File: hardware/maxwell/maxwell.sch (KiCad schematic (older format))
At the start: 29 parts

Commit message: Adding finalized PCB layout.
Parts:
- removed J?: Charger Output, symbol USB_A
- removed U?: MCP2515-I/ST, Housings_SSOP:TSSOP-20_4.4x6.5mm_Pitch0.65mm, symbol MCP2515-I/ST
- added J5: Charger Output, pbrook/Parts.pretty:JST-XH-4, symbol Conn_01x04
- added U1: MCP2515-E/ST-SOIC, Tinkerforge/kicad-libraries:SOIC-18, symbol MCP2515-E/ST-SOIC
- BZ1: renamed from BZ?; footprint (none) -> coddingtonbear/coddingtonbear.pretty:12mm_buzzer
- C1, C2, C3, C4, C5: renamed from C?; footprint (none) -> coddingtonbear/coddingtonbear.pretty:0805_Milling
- J1, J2: renamed from J?; footprint (none) -> pbrook/Parts.pretty:JST-XH-4
- J3: renamed from J?; footprint (none) -> pbrook/Parts.pretty:JST-XH-3
- J4: renamed from J?; footprint (none) -> KiCad/Pin_Headers.pretty:Pin_Header_Straight_2x03_Pitch2.54mm
- J6: renamed from J?; footprint (none) -> KiCad/Pin_Headers.pretty:Pin_Header_Straight_1x04_Pitch2.54mm
- Q1: renamed from Q?; footprint TO_SOT_Packages_SMD:SOT-23 -> adamgreig/agg-kicad/agg.pretty:SOT-23
- R1, R2, R3, R4, R5, R6, R7, R8, R9: renamed from R?; footprint (none) -> coddingtonbear/coddingtonbear.pretty:0805_Milling
- U2: renamed from U?; footprint Housings_SOIC:SOIC-8_3.9x4.9mm_Pitch1.27mm -> adamgreig/agg-kicad/agg.pretty:SOIC-8
- U3: renamed from U?; footprint (none) -> pelrun/libKiCad/footprint/w_rf_modules.pretty:ITEAD_HC-05
- U4: renamed from U?; footprint (none) -> coddingtonbear/coddingtonbear.pretty:SIM800L_Breakout
- U5: renamed from U?; footprint (none) -> coddingtonbear/coddingtonbear.pretty:BOOST_LM2596_3A
- U6: renamed from U?; footprint (none) -> kicad-castellated-breakouts:SSOP8-1.27MM-CASTELLATED
- Y1: renamed from Y?; footprint (none) -> SchrodingersGat/Components.pretty:crystal_hc-49s
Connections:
- wire segments 111 -> 106

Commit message: Updating schematic to add reverse polarity protection, higher-current diodes for zener limiting, and a low-side n-channel mosfet for enabling/disabling devices receiving direct battery power (limiting that quiescent current as much as possible).
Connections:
- net GND: no longer BZ1.2 (+), C5.2, J3.3 (Pin_3), J5.4 (Pin_4), R2.1, R4.2, U4.5 (GND), U5.2 (IN-), U5.4 (OUT-), U6.1 (PAD)
- new net GNDPWR: BZ1.2 (+), C5.2, J3.3 (Pin_3), J5.4 (Pin_4), R2.1, R4.2, U4.5 (GND), U5.2 (IN-), U5.4 (OUT-), U6.1 (PAD)
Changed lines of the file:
@@
 Connection ~ 9550 5750
 Connection ~ 9900 5550
-$Comp
-L GND #PWR05
-U 1 1 5A18D511
-P 9600 2900
-F 0 "#PWR05" H 9600 2650 50  0001 C CNN
-F 1 "GND" H 9605 2727 50  0000 C CNN
-F 2 "" H 9600 2900 50  0001 C CNN
-F 3 "" H 9600 2900 50  0001 C CNN
-	1    9600 2900
-	1    0    0    -1
-$EndComp
 $Sheet
 S 800  750  1250 700
@@
 	1    0    0    -1
 $EndComp
-$Comp
-L GND #PWR016
-U 1 1 5A2444F6
-P 6750 3950
-F 0 "#PWR016" H 6750 3700 50  0001 C CNN
-F 1 "GND" H 6755 3777 50  0000 C CNN
-F 2 "" H 6750 3950 50  0001 C CNN
-F 3 "" H 6750 3950 50  0001 C CNN
-	1    6750 3950
-	1    0    0    -1
-$EndComp
 Text GLabel 5850 3950 0    60   Input ~ 0
 GSM_TXD
@@
 F 3 "" V 3975 4000 50  0001 C CNN
 	1    4000 3900
-	1    0    0    -1
-$EndComp
-$Comp
-L GND #PWR017
-U 1 1 5A2492AA
-P 3950 4650
-F 0 "#PWR017" H 3950 4400 50  0001 C CNN
-F 1 "GND" H 3955 4477 50  0000 C CNN
-F 2 "" H 3950 4650 50  0001 C CNN
-F 3 "" H 3950 4650 50  0001 C CNN
-	1    3950 4650
 	1    0    0    -1
 $EndComp
@@
 	1    0    0    -1
 $EndComp
-$Comp
-L GND #PWR020
-U 1 1 5A24AA2F
-P 6000 5050
-F 0 "#PWR020" H 6000 4800 50  0001 C CNN
-F 1 "GND" H 6005 4877 50  0000 C CNN
-F 2 "" H 6000 5050 50  0001 C CNN
-F 3 "" H 6000 5050 50  0001 C CNN
-	1    6000 5050
-	1    0    0    -1
-$EndComp
 Text GLabel 6000 4950 0    60   Input ~ 0
 NEOPIXEL
@@
 	1    0    0    -1
 $EndComp
+$Comp
+L GNDPWR #PWR05
+U 1 1 5A258FF8
+P 6750 3950
+F 0 "#PWR05" H 6750 3750 50  0001 C CNN
+F 1 "GNDPWR" H 6754 4024 50  0000 C CNN
+F 2 "" H 6750 3900 50  0001 C CNN
+F 3 "" H 6750 3900 50  0001 C CNN
+	1    6750 3950
+	1    0    0    -1
+$EndComp
+$Comp
+L GNDPWR #PWR016
+U 1 1 5A259062
+P 3950 4650
+F 0 "#PWR016" H 3950 4450 50  0001 C CNN
+F 1 "GNDPWR" H 3954 4724 50  0000 C CNN
+F 2 "" H 3950 4600 50  0001 C CNN
+F 3 "" H 3950 4600 50  0001 C CNN
+	1    3950 4650
+	1    0    0    -1
+$EndComp
+$Comp
+L GNDPWR #PWR017
+U 1 1 5A2590C5
+P 6000 5050
+F 0 "#PWR017" H 6000 4850 50  0001 C CNN
+F 1 "GNDPWR" H 6004 5124 50  0000 C CNN
+F 2 "" H 6000 5000 50  0001 C CNN
+F 3 "" H 6000 5000 50  0001 C CNN
+	1    6000 5050
+	1    0    0    -1
+$EndComp
+$Comp
+L GNDPWR #PWR020
+U 1 1 5A259128
+P 9600 2900
+F 0 "#PWR020" H 9600 2700 50  0001 C CNN
+F 1 "GNDPWR" H 9604 2974 50  0000 C CNN
+F 2 "" H 9600 2850 50  0001 C CNN
+F 3 "" H 9600 2850 50  0001 C CNN
+	1    9600 2900
+	1    0    0    -1
+$EndComp

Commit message: More minor changes and fixes.
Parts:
- removed J1: Canbus 1, pbrook/Parts.pretty:JST-XH-4, symbol Conn_01x04
- removed J2: Canbus 2, pbrook/Parts.pretty:JST-XH-4, symbol Conn_01x04
- added J1: Canbus 1, KiCad/Connectors_JST.pretty:JST_XH_B05B-XH-A_05x2.50mm_Straight, symbol Conn_01x05
- added J2: Canbus 2, KiCad/Connectors_JST.pretty:JST_XH_B05B-XH-A_05x2.50mm_Straight, symbol Conn_01x05
- added R27: 1k, coddingtonbear/coddingtonbear.pretty:0805_Milling, symbol R
- added R28: 10k, coddingtonbear/coddingtonbear.pretty:0805_Milling, symbol R
- added R29: 330, coddingtonbear/coddingtonbear.pretty:0805_Milling, symbol R
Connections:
- net +BATT: now also J1.2 (Pin_2), J2.2 (Pin_2)
- net BT_KEY: now also R29.1; no longer U3.26 (PIO3)
- net GND: now also J1.5 (Pin_5), J2.5 (Pin_5), R28.1
- net GNDPWR: now also R6.2
- net at C5.1, U5.3 (OUT+), U6.3 (IN): no longer R6.2
- net TXCAN: now reaches U1.1 (TXCAN), U2.1 (D)
- net RXCAN: now reaches U1.2 (RXCAN), U2.4 (R)
- net CAN-: now reaches U2.6 (CANL)
- net CAN-: now also J1.4 (Pin_4), J2.4 (Pin_4)
- net CAN+: now reaches U2.7 (CANH)
- net CAN+: now also J1.3 (Pin_3), J2.3 (Pin_3)
- net at U3.29 (PIO6): now also R27.2
- net at U3.34 (PIO11): now also R28.2, R29.2
- net ~DISABLE_USB_OUT renamed ENABLE_USB_OUT
- new net POWER_ON: J1.1 (Pin_1), J2.1 (Pin_1), R27.1
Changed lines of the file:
@@
 	8600 2050 9700 2050
-Wire Wire Line
-	8600 850  8600 2050
 Wire Wire Line
 	8600 1450 8800 1450
@@
 Wire Wire Line
 	9150 850  8600 850
-Connection ~ 8600 1450
 Text GLabel 9850 850  2    60   Input ~ 0
-~DISABLE_USB_OUT
+ENABLE_USB_OUT
 Connection ~ 9800 850
 $Comp
@@
 	3350 6700 3900 6700
 Connection ~ 3900 6700
-$Comp
-L Conn_01x04 J1
-U 1 1 5A228A9B
-P 5100 6100
-F 0 "J1" H 5180 6092 50  0000 L CNN
-F 1 "Canbus 1" H 5180 6001 50  0000 L CNN
-F 2 "pbrook/Parts.pretty:JST-XH-4" H 5100 6100 50  0001 C CNN
-F 3 "" H 5100 6100 50  0001 C CNN
-	1    5100 6100
-	1    0    0    -1
-$EndComp
-$Comp
-L Conn_01x04 J2
-U 1 1 5A228ADF
-P 5100 6700
-F 0 "J2" H 5180 6692 50  0000 L CNN
-F 1 "Canbus 2" H 5180 6601 50  0000 L CNN
-F 2 "pbrook/Parts.pretty:JST-XH-4" H 5100 6700 50  0001 C CNN
-F 3 "" H 5100 6700 50  0001 C CNN
-	1    5100 6700
-	1    0    0    -1
-$EndComp
 Wire Wire Line
 	4300 6100 4900 6100
@@
 Wire Wire Line
 	8800 3650 10000 3650
-Text GLabel 5950 2450 2    60   BiDi ~ 0
+Text GLabel 5900 2450 2    60   BiDi ~ 0
 BOOT0
-Text GLabel 5400 1850 2    60   Input ~ 0
+Text GLabel 6100 2650 2    60   Input ~ 0
 BT_KEY
 $Comp
@@
 	0    1    1    0
 $EndComp
-Wire Wire Line
-	5500 2450 5400 2450
-Wire Wire Line
-	5800 2450 5950 2450
 $Comp
 L +BATT #PWR021
@@
 	1    0    0    -1
 $EndComp
+$Comp
+L Conn_01x05 J1
+U 1 1 5A25E0A2
+P 5100 6100
+F 0 "J1" H 5180 6142 50  0000 L CNN
+F 1 "Canbus 1" H 5180 6051 50  0000 L CNN
+F 2 "KiCad/Connectors_JST.pretty:JST_XH_B05B-XH-A_05x2.50mm_Straight" H 5100 6100 50  0001 C CNN
+F 3 "" H 5100 6100 50  0001 C CNN
+	1    5100 6100
+	1    0    0    -1
+$EndComp
+$Comp
+L Conn_01x05 J2
+U 1 1 5A25E262
+P 5100 6700
+F 0 "J2" H 5180 6742 50  0000 L CNN
+F 1 "Canbus 2" H 5180 6651 50  0000 L CNN
+F 2 "KiCad/Connectors_JST.pretty:JST_XH_B05B-XH-A_05x2.50mm_Straight" H 5100 6700 50  0001 C CNN
+F 3 "" H 5100 6700 50  0001 C CNN
+	1    5100 6700
+	1    0    0    -1
+$EndComp
+Text GLabel 4800 5900 1    60   Output ~ 0
+POWER_ON
+Wire Wire Line
+	4900 5900 4800 5900
+Wire Wire Line
+	4800 5900 4800 6500
+Wire Wire Line
+	4800 6500 4900 6500
+Text Label 4350 6100 0    60   ~ 0
+CAN+
+Text Label 4350 6200 0    60   ~ 0
+CAN-
+Text Label 2850 6000 0    60   ~ 0
+RXCAN
+Text Label 2850 6100 0    60   ~ 0
+TXCAN
+Wire Wire Line
+	5800 2450 5900 2450
+Text GLabel 5700 2150 2    60   Output ~ 0
+POWER_ON
+$Comp
+L R R27
+U 1 1 5A263D2E
+P 5550 2150
+F 0 "R27" H 5620 2196 50  0000 L CNN
+F 1 "1k" H 5620 2105 50  0000 L CNN
+F 2 "coddingtonbear/coddingtonbear.pretty:0805_Milling" V 5480 2150 50  0001 C CNN
+F 3 "" H 5550 2150 50  0001 C CNN
+	1    5550 2150
+	0    1    1    0
+$EndComp
+Wire Wire Line
+	8600 850  8600 1250
+Connection ~ 8600 1250
+Wire Wire Line
+	8600 1450 8600 2050
+$Comp
+L R R28
+U 1 1 5A265BD2
+P 5700 2850
+F 0 "R28" H 5770 2896 50  0000 L CNN
+F 1 "10k" H 5770 2805 50  0000 L CNN
+F 2 "coddingtonbear/coddingtonbear.pretty:0805_Milling" V 5630 2850 50  0001 C CNN
+F 3 "" H 5700 2850 50  0001 C CNN
+	1    5700 2850
+	0    1    1    0
+$EndComp
+$Comp
+L GND #PWR052
+U 1 1 5A265CDC
+P 5850 2850
+F 0 "#PWR052" H 5850 2600 50  0001 C CNN
+F 1 "GND" H 5855 2677 50  0000 C CNN
+F 2 "" H 5850 2850 50  0001 C CNN
+F 3 "" H 5850 2850 50  0001 C CNN
+	1    5850 2850
+	1    0    0    -1
+$EndComp
+Wire Wire Line
+	5400 2650 5800 2650
+Wire Wire Line
+	5550 2850 5500 2850
+Wire Wire Line
+	5500 2850 5500 2650
+Connection ~ 5500 2650
+Wire Wire Line
+	5500 2450 5400 2450
+$Comp
+L R R29
+U 1 1 5A266BEB
+P 5950 2650
+F 0 "R29" H 6020 2696 50  0000 L CNN
+F 1 "330" H 6020 2605 50  0000 L CNN
+F 2 "coddingtonbear/coddingtonbear.pretty:0805_Milling" V 5880 2650 50  0001 C CNN
+F 3 "" H 5950 2650 50  0001 C CNN
+	1    5950 2650
+	0    1    1    0
+$EndComp
 $EndSCHEMATC

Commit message: More fixes, additions, improvements.
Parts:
- added R31: 330, coddingtonbear/coddingtonbear.pretty:0805_Milling, symbol R
- added R32: 10k, coddingtonbear/coddingtonbear.pretty:0805_Milling, symbol R
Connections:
- net +3V3: now also R32.1
- net BOOT0: now also R5.1; no longer J4.3 (Pin_3), R5.2
- net BOOT1: no longer J4.4 (Pin_4)
- net GND: no longer R5.1, R9.1
- net NEOPIXEL: now also R31.2; no longer J3.2 (Pin_2)
- net CAN_INT: now reaches U1.12 (~INT)
- net at U1.17 (~RESET): now also R32.2
- new net: J4.3 (Pin_3), R5.2
- new net: J4.4 (Pin_4), R9.1
- new net: J3.2 (Pin_2), R31.1
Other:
- moved on the sheet: R5, R9
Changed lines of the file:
@@
 L R R5
 U 1 1 5A1763A1
-P 8800 3950
-F 0 "R5" H 8870 3996 50  0000 L CNN
-F 1 "100k" H 8870 3905 50  0000 L CNN
-F 2 "coddingtonbear/coddingtonbear.pretty:0805_Milling" V 8730 3950 50  0001 C CNN
-F 3 "" H 8800 3950 50  0001 C CNN
-	1    8800 3950
-	1    0    0    -1
+P 8800 4100
+F 0 "R5" H 8870 4146 50  0000 L CNN
+F 1 "100k" H 8870 4055 50  0000 L CNN
+F 2 "coddingtonbear/coddingtonbear.pretty:0805_Milling" V 8730 4100 50  0001 C CNN
+F 3 "" H 8800 4100 50  0001 C CNN
+	1    8800 4100
+	0    -1   -1   0
 $EndComp
 $Comp
 L R R9
 U 1 1 5A1763F8
-P 10000 3950
-F 0 "R9" H 10070 3996 50  0000 L CNN
-F 1 "100k" H 10070 3905 50  0000 L CNN
-F 2 "coddingtonbear/coddingtonbear.pretty:0805_Milling" V 9930 3950 50  0001 C CNN
-F 3 "" H 10000 3950 50  0001 C CNN
-	1    10000 3950
-	1    0    0    -1
-$EndComp
-Text GLabel 10300 4100 2    60   BiDi ~ 0
+P 9600 4100
+F 0 "R9" H 9670 4146 50  0000 L CNN
+F 1 "100k" H 9670 4055 50  0000 L CNN
+F 2 "coddingtonbear/coddingtonbear.pretty:0805_Milling" V 9530 4100 50  0001 C CNN
+F 3 "" H 9600 4100 50  0001 C CNN
+	1    9600 4100
+	0    -1   -1   0
+$EndComp
+Text GLabel 9750 4100 2    60   BiDi ~ 0
 BOOT1
-Wire Wire Line
-	10000 3650 10000 3800
-Wire Wire Line
-	9450 4100 10300 4100
-Wire Wire Line
-	8600 4100 8950 4100
-Wire Wire Line
-	8800 3800 8800 3650
 $Comp
 L Conn_01x04 J6
@@
 Text GLabel 4200 1600 0    60   Output ~ 0
 RXD
-Text GLabel 8600 4100 0    60   BiDi ~ 0
+Text GLabel 8650 4100 0    60   BiDi ~ 0
 BOOT0
-Connection ~ 10000 4100
-Connection ~ 8800 4100
-$Comp
-L GND #PWR014
-U 1 1 5A23B2EB
-P 10000 3650
-F 0 "#PWR014" H 10000 3400 50  0001 C CNN
-F 1 "GND" V 10005 3522 50  0000 R CNN
-F 2 "" H 10000 3650 50  0001 C CNN
-F 3 "" H 10000 3650 50  0001 C CNN
-	1    10000 3650
-	0    -1   -1   0
-$EndComp
-Wire Wire Line
-	8800 3650 10000 3650
 Text GLabel 5900 2450 2    60   BiDi ~ 0
 BOOT0
@@
 	1    0    0    -1
 $EndComp
-Text GLabel 6000 4950 0    60   Input ~ 0
+Text GLabel 5700 4950 0    60   Input ~ 0
 NEOPIXEL
 Wire Wire Line
 	6000 4850 6200 4850
-Wire Wire Line
-	6200 4950 6000 4950
 Wire Wire Line
 	6000 5050 6200 5050
@@
 	0    1    1    0
 $EndComp
+$Comp
+L R R31
+U 1 1 5A271748
+P 5850 4950
+F 0 "R31" H 5920 4996 50  0000 L CNN
+F 1 "330" H 5920 4905 50  0000 L CNN
+F 2 "coddingtonbear/coddingtonbear.pretty:0805_Milling" V 5780 4950 50  0001 C CNN
+F 3 "" H 5850 4950 50  0001 C CNN
+	1    5850 4950
+	0    1    1    0
+$EndComp
+Wire Wire Line
+	6000 4950 6200 4950
+$Comp
+L R R32
+U 1 1 5A271FA2
+P 3050 7050
+F 0 "R32" H 3120 7096 50  0000 L CNN
+F 1 "10k" H 3120 7005 50  0000 L CNN
+F 2 "coddingtonbear/coddingtonbear.pretty:0805_Milling" V 2980 7050 50  0001 C CNN
+F 3 "" H 3050 7050 50  0001 C CNN
+	1    3050 7050
+	1    0    0    -1
+$EndComp
+$Comp
+L +3V3 #PWR034
+U 1 1 5A271FFF
+P 3050 6900
+F 0 "#PWR034" H 3050 6750 50  0001 C CNN
+F 1 "+3V3" H 3065 7073 50  0000 C CNN
+F 2 "" H 3050 6900 50  0001 C CNN
+F 3 "" H 3050 6900 50  0001 C CNN
+	1    3050 6900
+	1    0    0    -1
+$EndComp
+Wire Wire Line
+	2800 7200 3050 7200
+Text GLabel 2800 6600 2    60   Output ~ 0
+CAN_INT
 $EndSCHEMATC

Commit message: Fixed just...an unbelievable number of bugs.
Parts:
- removed U6: TPS2511, kicad-castellated-breakouts:SSOP8-1.27MM-CASTELLATED, symbol TPS2511
- added U11: TPS2514, adamgreig/agg-kicad/agg.pretty:SOT-23-6, symbol TPS2514
- added U6: STT3P2UH7, adamgreig/agg-kicad/agg.pretty:SOT-23-6, symbol STT3P2UH7
- R4: value 25k -> >35
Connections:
- net ENABLE_USB_OUT is gone; now on an unnamed net: R6.1
- net +BATT: now also BZ1.1 (-); no longer Q1.3 (D)
- net GND: now also R2.1, R4.1
- net GNDPWR: now also U11.2 (GND); no longer BZ1.2 (+), R2.1, R4.2, R6.2
- net at C5.1, U5.3 (OUT+): now also U11.5 (IN), U6.4 (SRC)
- net at J5.3 (Pin_3): now also U11.6 (DM1)
- net at J5.2 (Pin_2): now also U11.1 (DP1)
- net at J5.1 (Pin_1): now also U6.1 (DRAIN), U6.2 (DRAIN), U6.5 (DRAIN), U6.6 (DRAIN)
- net at Q1.2 (S): now also R4.2; no longer BZ1.1 (-)
- new net: BZ1.2 (+), Q1.3 (D)
- new net ~ENABLE_USB_OUT: R6.2, U6.3 (GATE)
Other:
- note removed: "Tune to 5V"
- moved on the sheet: C5, J5, Q1, R2, R6, U5

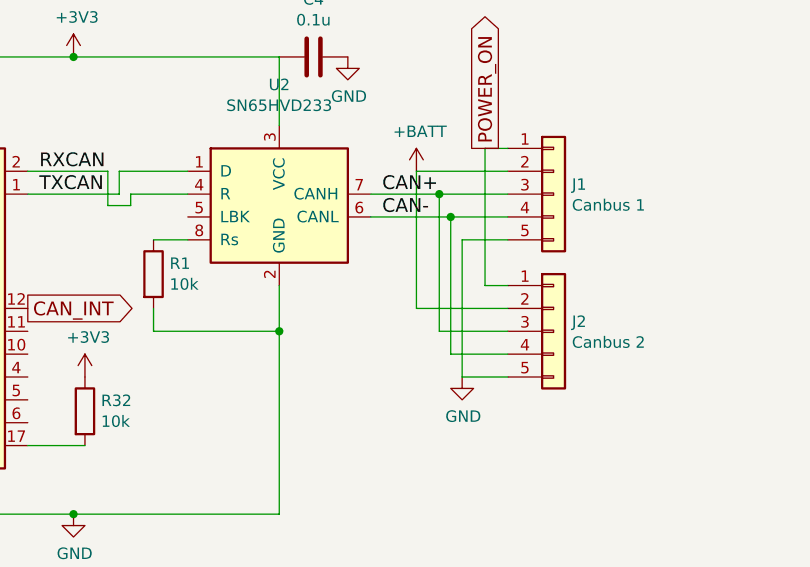
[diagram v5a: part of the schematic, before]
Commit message: Adding CANBus termination resistors.
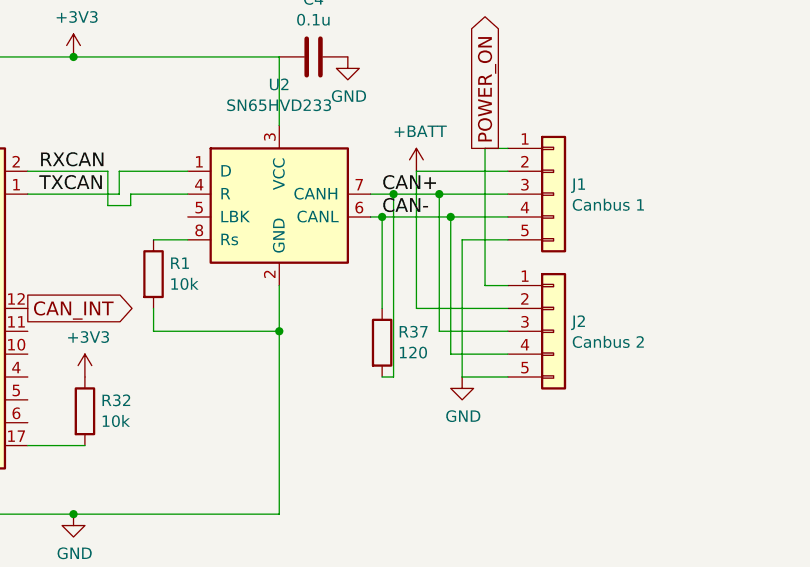
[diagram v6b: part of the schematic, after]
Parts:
- added R37: 120, coddingtonbear/coddingtonbear.pretty:0805_Milling, symbol R
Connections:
- net CAN+: now also R37.2
- net CAN-: now also R37.1
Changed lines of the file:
@@
 	8750 2200 8750 2300
 Connection ~ 8750 2300
+$Comp
+L R R37
+U 1 1 5A2B653B
+P 4350 6750
+F 0 "R37" H 4420 6796 50  0000 L CNN
+F 1 "120" H 4420 6705 50  0000 L CNN
+F 2 "coddingtonbear/coddingtonbear.pretty:0805_Milling" V 4280 6750 50  0001 C CNN
+F 3 "" H 4350 6750 50  0001 C CNN
+	1    4350 6750
+	1    0    0    -1
+$EndComp
+Wire Wire Line
+	4350 6200 4350 6600
+Connection ~ 4350 6200
+Wire Wire Line
+	4400 6100 4400 6900
+Wire Wire Line
+	4400 6900 4350 6900
+Connection ~ 4400 6100
 $EndSCHEMATC
